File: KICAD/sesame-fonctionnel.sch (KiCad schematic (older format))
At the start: 8 parts

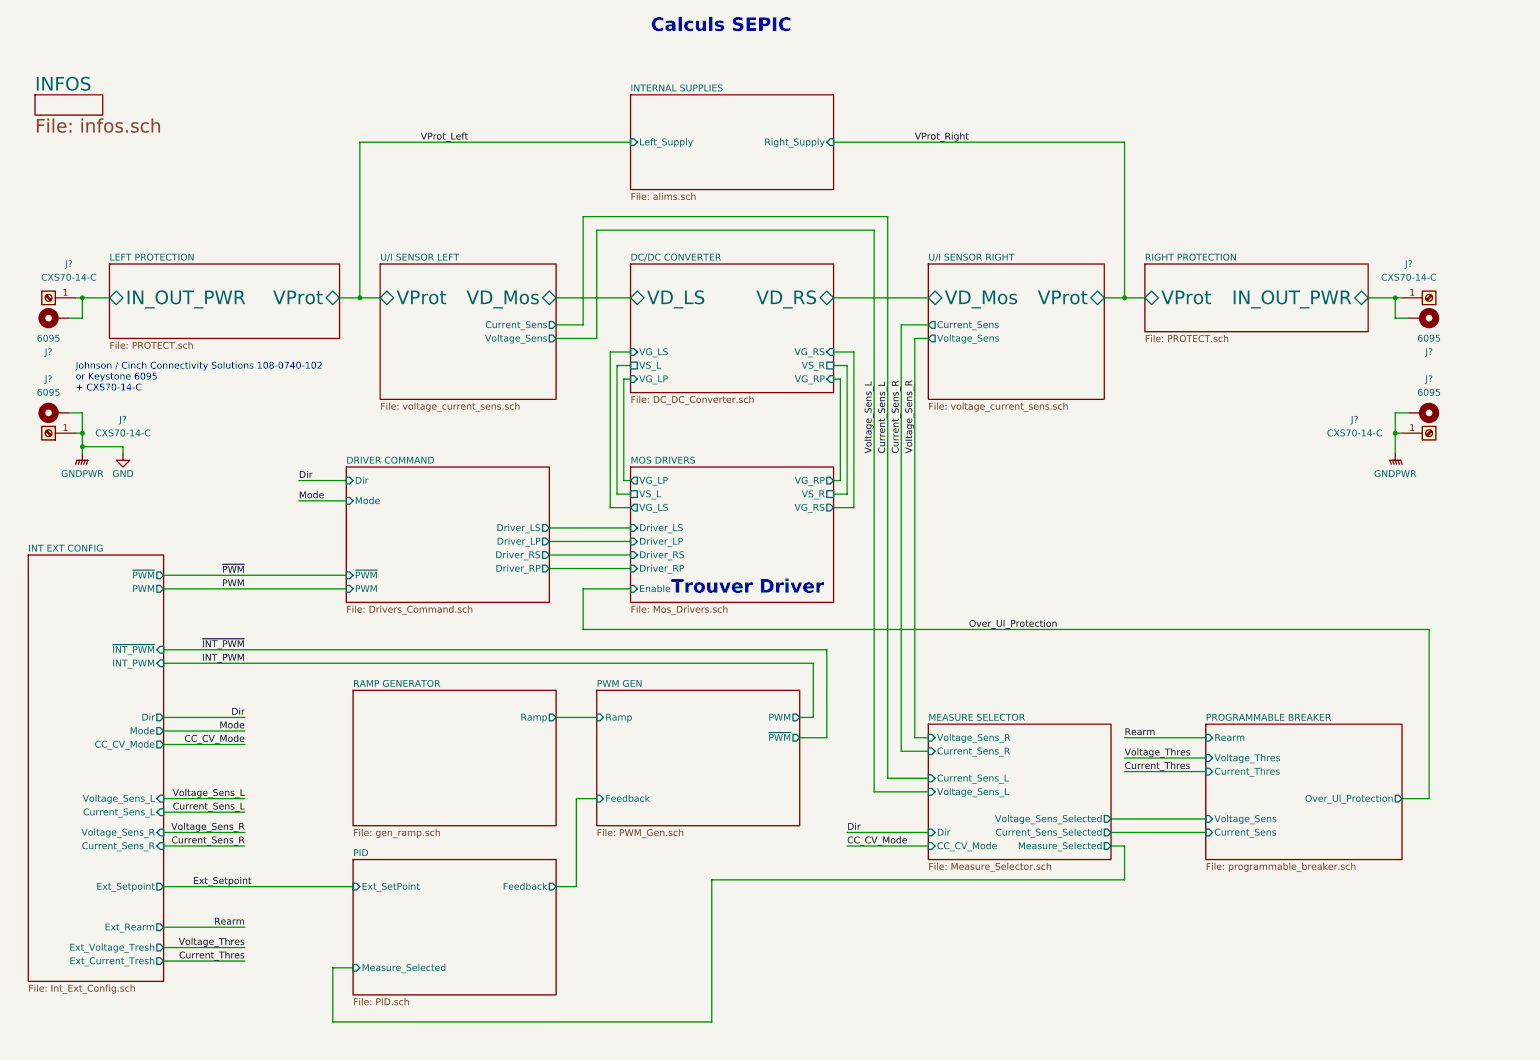
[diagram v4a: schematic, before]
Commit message: drivers draft + clean and minors changes
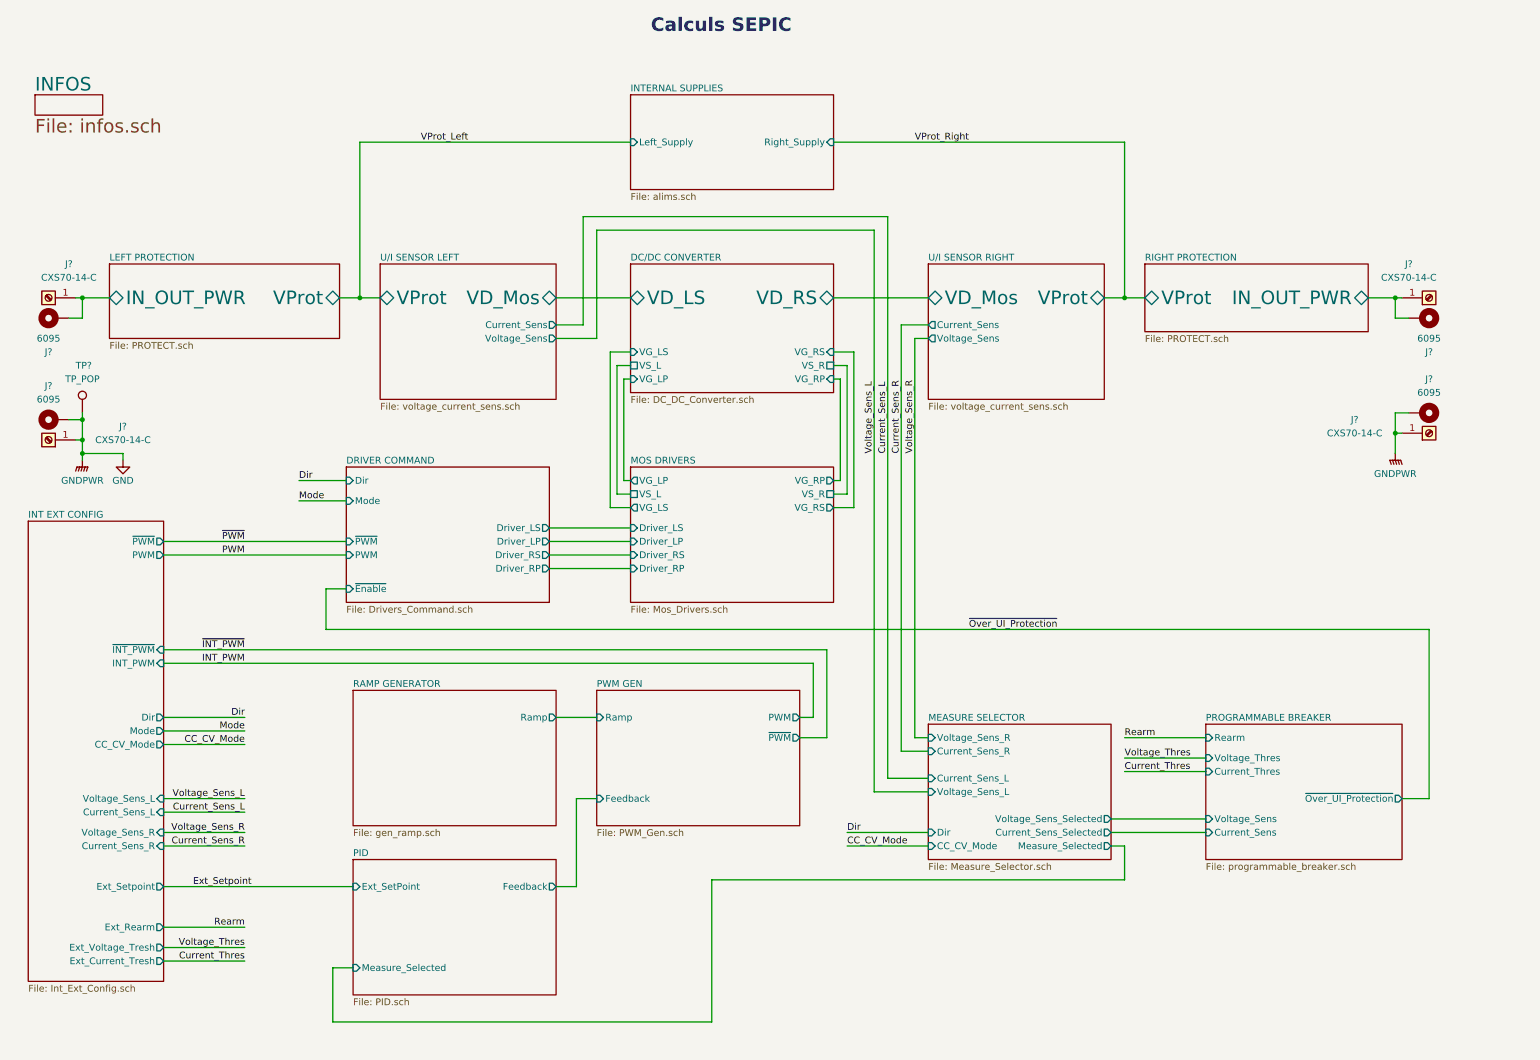
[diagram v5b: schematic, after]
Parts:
- added TP?: TP_POP, symbol Connector:TestPoint
- J? (x2): footprint (none) -> Sesame_footprint:CXS70-14-C
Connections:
- net GND: now also TP?.1
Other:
- note removed: "Johnson / Cinch Connectivity Solutions 108-0740-102\nor Keystone 6095\n+ CXS70-14-C"
- note removed: "Trouver Driver"
- moved on the sheet: J?
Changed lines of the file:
@@
 L power:GND #PWR0104
 U 1 1 60FAC5D8
-P 1300 3350
-F 0 "#PWR0104" H 1300 3100 50  0001 C CNN
-F 1 "GND" H 1300 3200 50  0000 C CNN
-F 2 "" H 1300 3350 50  0001 C CNN
-F 3 "" H 1300 3350 50  0001 C CNN
-	1    1300 3350
+P 1300 3400
+F 0 "#PWR0104" H 1300 3150 50  0001 C CNN
+F 1 "GND" H 1300 3250 50  0000 C CNN
+F 2 "" H 1300 3400 50  0001 C CNN
+F 3 "" H 1300 3400 50  0001 C CNN
+	1    1300 3400
 	-1   0    0    -1
 $EndComp
 Text Label 7550 4650 0    50   ~ 0
-Over_UI_Protection
+~Over_UI_Protection
 $Sheet
 S 3000 6350 1500 1000
@@
 F2 "Current_Sens" I L 9300 6150 50
 F3 "Voltage_Sens" I L 9300 6050 50
-F4 "Over_UI_Protection" O R 10750 5900 50
+F4 "~Over_UI_Protection" O R 10750 5900 50
 F5 "Rearm" I L 9300 5450 50
 F6 "Current_Thres" I L 9300 5700 50
@@
 $EndSheet
 Wire Wire Line
-	4700 4350 4700 4650
+	2800 4350 2800 4650
 $Sheet
 S 2950 3450 1500 1000
@@
 F4 "Driver_RS" O R 4450 4100 50
 F5 "Driver_RP" O R 4450 4200 50
-F6 "PWM" I L 2950 4350 50
-F7 "~PWM" I L 2950 4250 50
+F6 "PWM" I L 2950 4100 50
+F7 "~PWM" I L 2950 4000 50
 F8 "Dir" I L 2950 3550 50
 F9 "Mode" I L 2950 3700 50
+F10 "~Enable" I L 2950 4350 50
 $EndSheet
 Text Label 2200 4900 2    50   ~ 0
@@
 F2 "Ramp" O R 4500 5300 50
 $EndSheet
-Text Notes 950  2900 0    50   ~ 0
-Johnson / Cinch Connectivity Solutions 108-0740-102\nor Keystone 6095\n+ CXS70-14-C
 $Comp
 L power:GNDPWR #PWR?
 U 1 1 6140956C
-P 1000 3350
-F 0 "#PWR?" H 1000 3150 50  0001 C CNN
-F 1 "GNDPWR" H 1000 3200 50  0000 C CNN
-F 2 "" H 1000 3300 50  0001 C CNN
-F 3 "" H 1000 3300 50  0001 C CNN
-	1    1000 3350
+P 1000 3400
+F 0 "#PWR?" H 1000 3200 50  0001 C CNN
+F 1 "GNDPWR" H 1000 3250 50  0000 C CNN
+F 2 "" H 1000 3350 50  0001 C CNN
+F 3 "" H 1000 3350 50  0001 C CNN
+	1    1000 3400
 	1    0    0    -1
 $EndComp
 Wire Wire Line
-	1000 3200 1000 3300
-Connection ~ 1000 3200
-Wire Wire Line
-	1300 3350 1300 3300
-Wire Wire Line
-	1300 3300 1000 3300
-Connection ~ 1000 3300
-Wire Wire Line
-	1000 3300 1000 3350
-Wire Wire Line
-	1000 3200 950  3200
-Wire Wire Line
-	1000 3050 1000 3200
-Wire Wire Line
-	900  3050 1000 3050
+	1000 3250 1000 3350
+Connection ~ 1000 3250
+Wire Wire Line
+	1300 3400 1300 3350
+Wire Wire Line
+	1300 3350 1000 3350
+Connection ~ 1000 3350
+Wire Wire Line
+	1000 3350 1000 3400
+Wire Wire Line
+	1000 3250 950  3250
 $Comp
 L Mechanical:MountingHole_Pad J?
 U 1 1 6142C008
-P 800 3050
-F 0 "J?" V 1050 3100 50  0000 C CNN
-F 1 "6095" V 950 3100 50  0000 C CNN
-F 2 "" H 800 3050 50  0001 C CNN
-F 3 "~" H 800 3050 50  0001 C CNN
-	1    800  3050
+P 800 3100
+F 0 "J?" V 1050 3150 50  0000 C CNN
+F 1 "6095" V 950 3150 50  0000 C CNN
+F 2 "" H 800 3100 50  0001 C CNN
+F 3 "~" H 800 3100 50  0001 C CNN
+	1    800  3100
 	0    -1   -1   0
 $EndComp
@@
 L Connector:Screw_Terminal_01x01 J?
 U 1 1 6142C002
-P 750 3200
-F 0 "J?" H 200 3100 50  0000 C CNN
-F 1 "CXS70-14-C" H 200 3200 50  0000 C CNN
-F 2 "" H 750 3200 50  0001 C CNN
-F 3 "~" H 750 3200 50  0001 C CNN
-	1    750  3200
+P 750 3250
+F 0 "J?" H 200 3150 50  0000 C CNN
+F 1 "CXS70-14-C" H 200 3250 50  0000 C CNN
+F 2 "Sesame_footprint:CXS70-14-C" H 750 3250 50  0001 C CNN
+F 3 "~" H 750 3250 50  0001 C CNN
+	1    750  3250
 	-1   0    0    1
 $EndComp
@@
 	0    -1   -1   0
 $EndComp
-$Comp
-L Connector:Screw_Terminal_01x01 J?
-U 1 1 61427119
-P 750 2200
-F 0 "J?" H 600 1950 50  0000 C CNN
-F 1 "CXS70-14-C" H 600 2050 50  0000 C CNN
-F 2 "Sesame_footprint:CXS70-14-C" H 750 2200 50  0001 C CNN
-F 3 "~" H 750 2200 50  0001 C CNN
-	1    750  2200
-	-1   0    0    1
-$EndComp
 Wire Wire Line
 	1000 2200 1200 2200
@@
 Wire Wire Line
 	4450 3900 5050 3900
-Wire Wire Line
-	5050 4350 4700 4350
 Wire Wire Line
 	6650 2700 6550 2700
@@
 F 0 "J?" H 10400 3100 50  0000 C CNN
 F 1 "CXS70-14-C" H 10400 3200 50  0000 C CNN
-F 2 "" H 10950 3200 50  0001 C CNN
+F 2 "Sesame_footprint:CXS70-14-C" H 10950 3200 50  0001 C CNN
 F 3 "~" H 10950 3200 50  0001 C CNN
 	1    10950 3200
@@
 F8 "Driver_RP" I L 5050 4200 50
 F9 "Driver_RS" I L 5050 4100 50
-F10 "Enable" I L 5050 4350 50
 F11 "VS_L" U L 5050 3650 50
 F12 "VS_R" U R 6550 3650 50
@@
 Wire Wire Line
 	6650 3650 6650 2700
-Text Notes 5350 4400 0    100  ~ 20
-Trouver Driver
 Wire Wire Line
 	6850 1700 6850 5850
@@
 Voltage_Sens_R
 Wire Wire Line
-	4700 4650 10950 4650
+	2800 4650 10950 4650
 Wire Wire Line
 	7050 2400 7050 5550
@@
 	2200 5500 1600 5500
 Wire Wire Line
-	1600 4250 2950 4250
-Wire Wire Line
-	1600 4350 2950 4350
+	1600 4000 2950 4000
+Wire Wire Line
+	1600 4100 2950 4100
 Wire Wire Line
 	1600 5400 2200 5400
@@
 	6500 4800 6500 5450
 $Sheet
-S 600  4100 1000 3150
+S 600  3850 1000 3400
 U 618748E2
 F0 "INT EXT CONFIG" 50
@@
 F8 "INT_PWM" I R 1600 4900 50
 F9 "~INT_PWM" I R 1600 4800 50
-F10 "PWM" O R 1600 4350 50
-F11 "~PWM" O R 1600 4250 50
+F10 "PWM" O R 1600 4100 50
+F11 "~PWM" O R 1600 4000 50
 F12 "CC_CV_Mode" O R 1600 5500 50
 F13 "Ext_Setpoint" O R 1600 6550 50
@@
 Wire Wire Line
 	6500 4800 1600 4800
-Text Label 2200 4250 2    50   ~ 0
+Text Label 2200 4000 2    50   ~ 0
 ~PWM
-Text Label 2200 4350 2    50   ~ 0
+Text Label 2200 4100 2    50   ~ 0
 PWM
 Text Notes 5200 250  0    100  ~ 20
@@
 F3 "Right_Supply" I R 6550 1050 50
 $EndSheet
+$Comp
+L Connector:Screw_Terminal_01x01 J?
+U 1 1 61427119
+P 750 2200
+F 0 "J?" H 600 1950 50  0000 C CNN
+F 1 "CXS70-14-C" H 600 2050 50  0000 C CNN
+F 2 "Sesame_footprint:CXS70-14-C" H 750 2200 50  0001 C CNN
+F 3 "~" H 750 2200 50  0001 C CNN
+	1    750  2200
+	-1   0    0    1
+$EndComp
+Connection ~ 1000 3100
+Wire Wire Line
+	900  3100 1000 3100
+Wire Wire Line
+	1000 3100 1000 3250
+$Comp
+L Connector:TestPoint TP?
+U 1 1 614ECCE3
+P 1000 3050
+AR Path="/614794AE/614ECCE3" Ref="TP?"  Part="1"
+AR Path="/61456C6A/614ECCE3" Ref="TP?"  Part="1"
+AR Path="/614ECCE3" Ref="TP?"  Part="1"
+F 0 "TP?" H 950 3400 50  0000 L CNN
+F 1 "TP_POP" H 1000 3300 50  0000 C CNN
+F 2 "" H 1200 3050 50  0001 C CNN
+F 3 "~" H 1200 3050 50  0001 C CNN
+	1    1000 3050
+	1    0    0    -1
+$EndComp
+Wire Wire Line
+	1000 3050 1000 3100
+Wire Wire Line
+	2950 4350 2800 4350
 $EndSCHEMATC

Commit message: driver + clean clean clean
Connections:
- net LEFT PROTECTION/IN_OUT_PWR renamed LEFT PROTECTION/IO_PWR
- net RIGHT PROTECTION/IN_OUT_PWR renamed RIGHT PROTECTION/IO_PWR

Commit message: review w/ jmt
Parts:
- gave numbers to parts that had none: 9
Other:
- note added: "<- VOIR PROBLEME DC"
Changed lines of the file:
@@
 	2850 7550 5650 7550
 $Comp
-L power:GND #PWR0104
+L power:GND #PWR01
 U 1 1 60FAC5D8
-P 1300 3400
-F 0 "#PWR0104" H 1300 3150 50  0001 C CNN
-F 1 "GND" H 1300 3250 50  0000 C CNN
-F 2 "" H 1300 3400 50  0001 C CNN
-F 3 "" H 1300 3400 50  0001 C CNN
-	1    1300 3400
+P 1000 3400
+F 0 "#PWR01" H 1000 3150 50  0001 C CNN
+F 1 "GND" H 1000 3250 50  0000 C CNN
+F 2 "" H 1000 3400 50  0001 C CNN
+F 3 "" H 1000 3400 50  0001 C CNN
+	1    1000 3400
 	-1   0    0    -1
 $EndComp
@@
 F2 "Ramp" O R 4500 5300 50
 $EndSheet
-$Comp
-L power:GNDPWR #PWR?
-U 1 1 6140956C
-P 1000 3400
-F 0 "#PWR?" H 1000 3200 50  0001 C CNN
-F 1 "GNDPWR" H 1000 3250 50  0000 C CNN
-F 2 "" H 1000 3350 50  0001 C CNN
-F 3 "" H 1000 3350 50  0001 C CNN
-	1    1000 3400
-	1    0    0    -1
-$EndComp
-Wire Wire Line
-	1000 3250 1000 3350
 Connection ~ 1000 3250
 Wire Wire Line
-	1300 3400 1300 3350
-Wire Wire Line
-	1300 3350 1000 3350
-Connection ~ 1000 3350
-Wire Wire Line
-	1000 3350 1000 3400
-Wire Wire Line
 	1000 3250 950  3250
 $Comp
-L Mechanical:MountingHole_Pad J?
+L Mechanical:MountingHole_Pad J4
 U 1 1 6142C008
 P 800 3100
-F 0 "J?" V 1050 3150 50  0000 C CNN
+F 0 "J4" V 1050 3150 50  0000 C CNN
 F 1 "6095" V 950 3150 50  0000 C CNN
 F 2 "" H 800 3100 50  0001 C CNN
@@
 $EndComp
 $Comp
-L Connector:Screw_Terminal_01x01 J?
+L Connector:Screw_Terminal_01x01 J2
 U 1 1 6142C002
 P 750 3250
-F 0 "J?" H 200 3150 50  0000 C CNN
-F 1 "CXS70-14-C" H 200 3250 50  0000 C CNN
+F 0 "J2" H 200 3200 50  0000 C CNN
+F 1 "CXS70-14-C" H 150 3300 50  0000 C CNN
 F 2 "Sesame_footprint:CXS70-14-C" H 750 3250 50  0001 C CNN
 F 3 "~" H 750 3250 50  0001 C CNN
@@
 $EndComp
 $Comp
-L Mechanical:MountingHole_Pad J?
+L Mechanical:MountingHole_Pad J3
 U 1 1 6142711F
 P 800 2350
-F 0 "J?" V 550 2400 50  0000 C CNN
+F 0 "J3" V 550 2400 50  0000 C CNN
 F 1 "6095" V 650 2400 50  0000 C CNN
 F 2 "" H 800 2350 50  0001 C CNN
@@
 $EndSheet
 $Comp
-L Mechanical:MountingHole_Pad J?
+L Mechanical:MountingHole_Pad J5
 U 1 1 61485222
 P 10900 2350
-F 0 "J?" V 10650 2400 50  0000 C CNN
+F 0 "J5" V 10650 2400 50  0000 C CNN
 F 1 "6095" V 10750 2400 50  0000 C CNN
 F 2 "" H 10900 2350 50  0001 C CNN
@@
 $EndComp
 $Comp
-L Connector:Screw_Terminal_01x01 J?
+L Connector:Screw_Terminal_01x01 J7
 U 1 1 6148521C
 P 10950 2200
-F 0 "J?" H 10800 1950 50  0000 C CNN
+F 0 "J7" H 10800 1950 50  0000 C CNN
 F 1 "CXS70-14-C" H 10800 2050 50  0000 C CNN
 F 2 "Sesame_footprint:CXS70-14-C" H 10950 2200 50  0001 C CNN
@@
 Wire Wire Line
 	6550 2800 6650 2800
-$Comp
-L power:GNDPWR #PWR?
-U 1 1 6156FACF
-P 10700 3350
-F 0 "#PWR?" H 10700 3150 50  0001 C CNN
-F 1 "GNDPWR" H 10700 3200 50  0000 C CNN
-F 2 "" H 10700 3300 50  0001 C CNN
-F 3 "" H 10700 3300 50  0001 C CNN
-	1    10700 3350
-	-1   0    0    -1
-$EndComp
 Connection ~ 10700 3200
 Wire Wire Line
@@
 	10800 3050 10700 3050
 $Comp
-L Mechanical:MountingHole_Pad J?
+L Mechanical:MountingHole_Pad J6
 U 1 1 6156FADE
 P 10900 3050
-F 0 "J?" V 11150 3100 50  0000 C CNN
+F 0 "J6" V 11150 3100 50  0000 C CNN
 F 1 "6095" V 11050 3100 50  0000 C CNN
 F 2 "" H 10900 3050 50  0001 C CNN
@@
 $EndComp
 $Comp
-L Connector:Screw_Terminal_01x01 J?
+L Connector:Screw_Terminal_01x01 J8
 U 1 1 6156FAE4
 P 10950 3200
-F 0 "J?" H 10400 3100 50  0000 C CNN
+F 0 "J8" H 10400 3100 50  0000 C CNN
 F 1 "CXS70-14-C" H 10400 3200 50  0000 C CNN
 F 2 "Sesame_footprint:CXS70-14-C" H 10950 3200 50  0001 C CNN
@@
 F0 "INTERNAL SUPPLIES" 50
 F1 "alims.sch" 50
-F2 "Left_Supply" I L 5050 1050 50
-F3 "Right_Supply" I R 6550 1050 50
-$EndSheet
-$Comp
-L Connector:Screw_Terminal_01x01 J?
+F2 "LEFT" I L 5050 1050 50
+F3 "RIGHT" I R 6550 1050 50
+$EndSheet
+$Comp
+L Connector:Screw_Terminal_01x01 J1
 U 1 1 61427119
 P 750 2200
-F 0 "J?" H 600 1950 50  0000 C CNN
+F 0 "J1" H 600 1950 50  0000 C CNN
 F 1 "CXS70-14-C" H 600 2050 50  0000 C CNN
 F 2 "Sesame_footprint:CXS70-14-C" H 750 2200 50  0001 C CNN
@@
 AR Path="/614794AE/614ECCE3" Ref="TP?"  Part="1"
 AR Path="/61456C6A/614ECCE3" Ref="TP?"  Part="1"
-AR Path="/614ECCE3" Ref="TP?"  Part="1"
-F 0 "TP?" H 950 3400 50  0000 L CNN
+AR Path="/614ECCE3" Ref="TP1"  Part="1"
+F 0 "TP1" H 950 3400 50  0000 L CNN
 F 1 "TP_POP" H 1000 3300 50  0000 C CNN
 F 2 "" H 1200 3050 50  0001 C CNN
@@
 Wire Wire Line
 	4650 4250 6850 4250
+$Comp
+L power:PWR_FLAG #FLG01
+U 1 1 61B60E72
+P 1400 3000
+F 0 "#FLG01" H 1400 3075 50  0001 C CNN
+F 1 "PWR_FLAG" H 1400 3173 50  0000 C CNN
+F 2 "" H 1400 3000 50  0001 C CNN
+F 3 "~" H 1400 3000 50  0001 C CNN
+	1    1400 3000
+	1    0    0    -1
+$EndComp
+Wire Wire Line
+	1400 3100 1000 3100
+Wire Wire Line
+	1400 3000 1400 3100
+Wire Wire Line
+	1000 3250 1000 3400
+$Comp
+L power:GND #PWR02
+U 1 1 61BCC559
+P 10700 3350
+F 0 "#PWR02" H 10700 3100 50  0001 C CNN
+F 1 "GND" H 10705 3177 50  0000 C CNN
+F 2 "" H 10700 3350 50  0001 C CNN
+F 3 "" H 10700 3350 50  0001 C CNN
+	1    10700 3350
+	1    0    0    -1
+$EndComp
+Text Notes 4800 3550 0    100  ~ 20
+<- VOIR PROBLEME DC
 $EndSCHEMATC
